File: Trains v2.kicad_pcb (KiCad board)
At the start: 2 copper layers, 200 x 50 mm, 28 parts, among them SW1 SW_SPST4, SW2 SW_SPST4

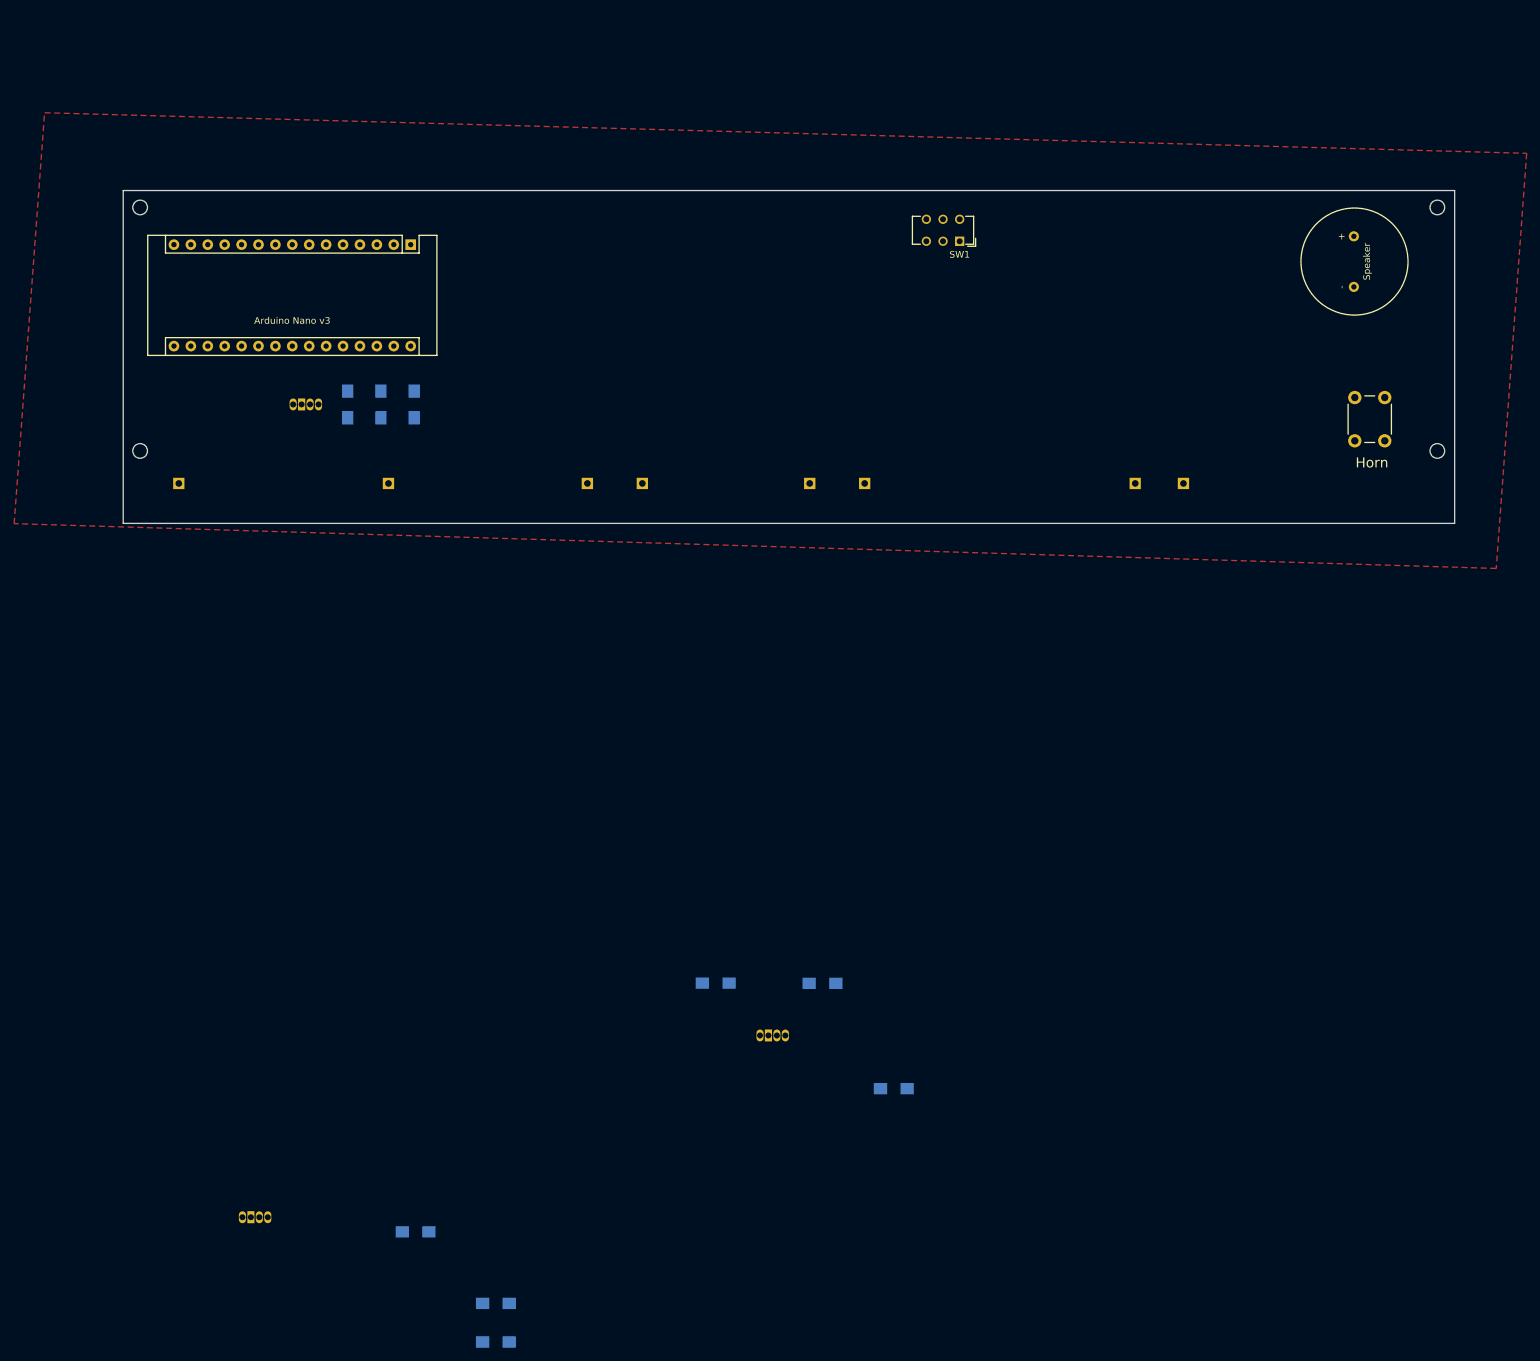
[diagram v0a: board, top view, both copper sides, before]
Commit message: Add & Align Pins
Add pins to all trains and set proper locations
Move RGB LEDs and resistors
Connect RGB LEDs to resistors and speaker to Arduino
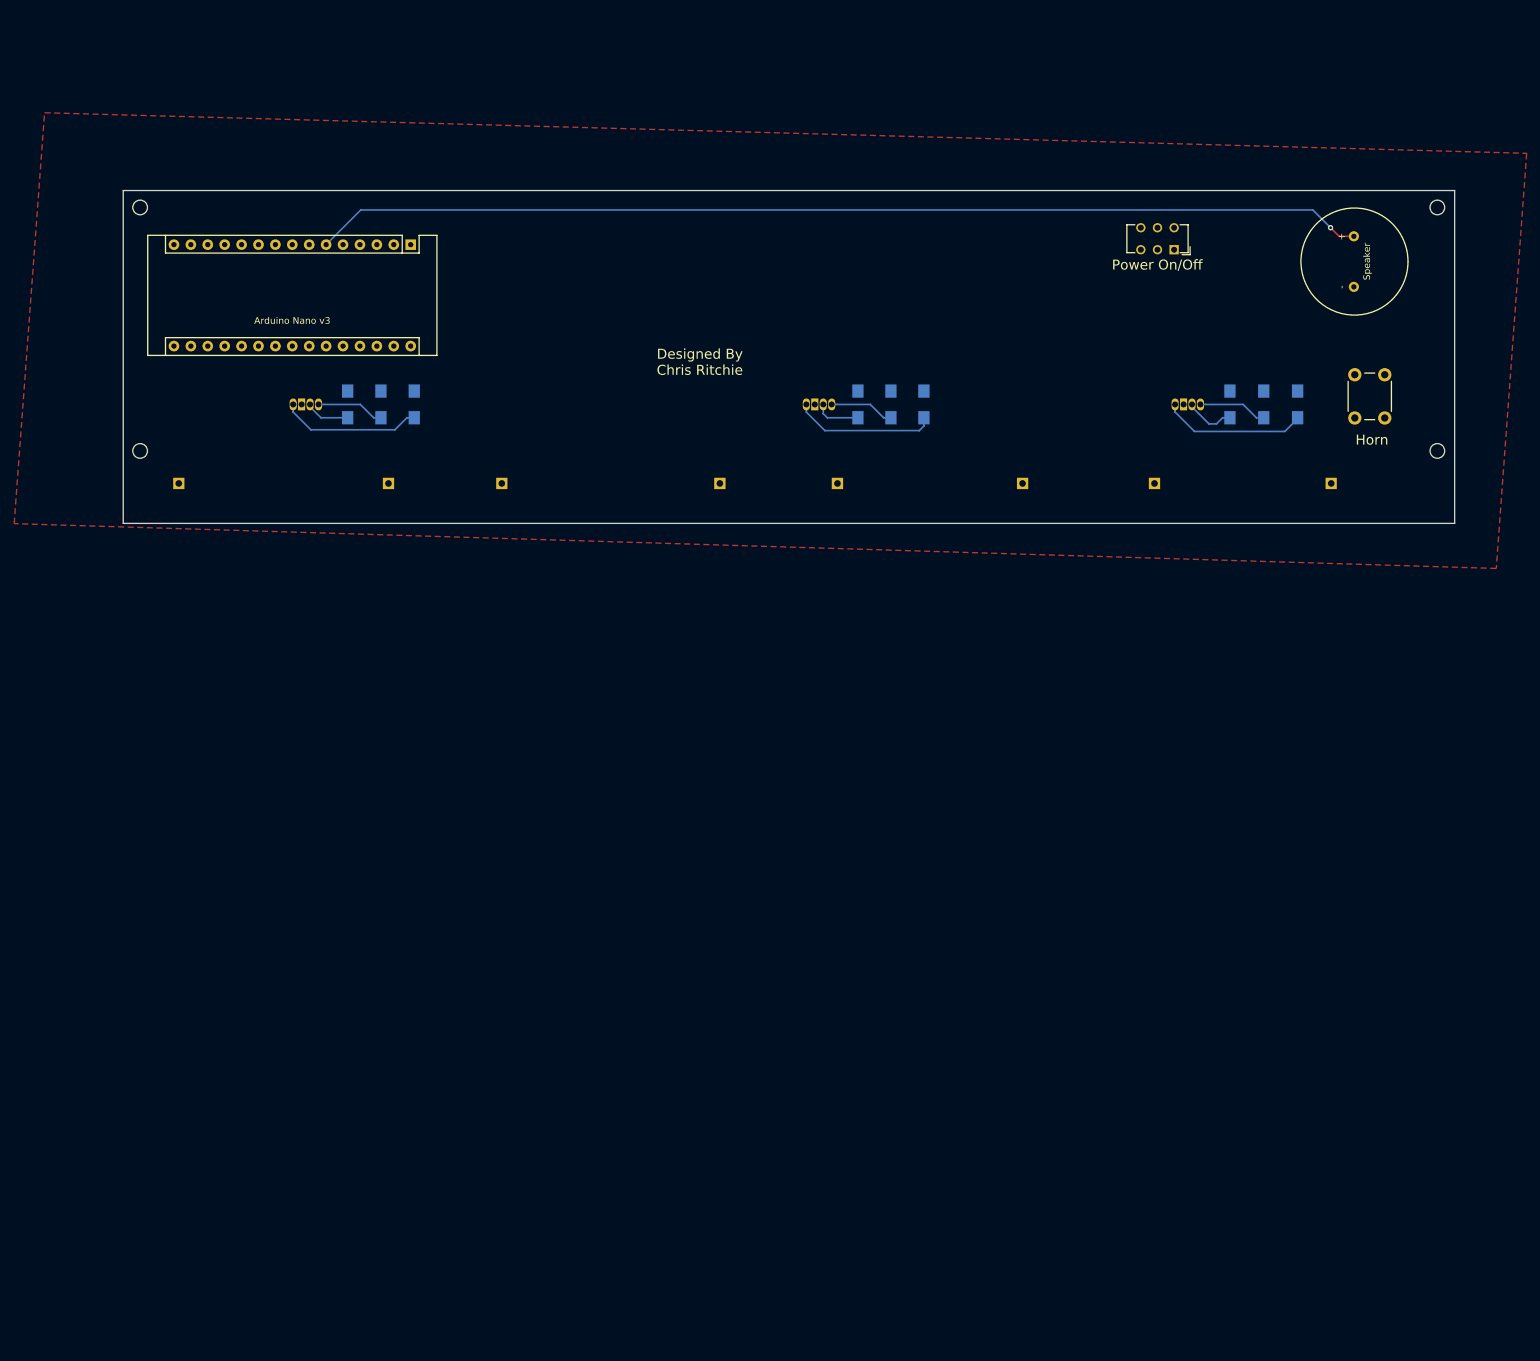
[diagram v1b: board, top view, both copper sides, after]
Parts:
- added G***: LOGO, logo:logoSolder, F.Cu at (80.0, 22.2)
- SW1: footprint Buttons_Switches_THT:SW_CuK_JS202011AQN_DPDT_Angled -> Buttons_Switches_THT:SW_CuK_JS202011CQN_DPDT_Straight
- moved R4 151.0 mm to (110.4, 32.1), turned to 90 degrees
- moved R6 149.6 mm to (120.3, 32.1), turned to 90 degrees
- moved D2 148.6 mm to (102.6, 32.1)
- moved R5 143.3 mm to (115.3, 32.1), turned to 90 degrees
- moved R9 119.3 mm to (176.4, 32.1), turned to 90 degrees
- moved R7 116.3 mm to (166.2, 32.1), turned to 90 degrees
- moved D3 113.5 mm to (158.0, 32.1)
- moved R8 109.3 mm to (171.3, 32.1), turned to 90 degrees
- moved SW1 32.2 mm to (157.9, 8.89)
- moved MK6 32.0 mm to (135.1, 44.0)
- moved MK8 29.4 mm to (181.5, 44.0)
- moved MK3 21.1 mm to (56.9, 44.0)
- moved MK4 19.9 mm to (89.6, 44.0)
- moved R1 5.00 mm to (33.7, 32.1)
- moved R2 5.00 mm to (38.7, 32.1)
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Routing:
- net /Speaker_Pin: track 0.00 -> 158.2 mm, vias 0 -> 1
- net Net-(D3-Pad1): track 0.00 -> 21.7 mm
- net Net-(D2-Pad1): track 0.00 -> 21.5 mm
- net Net-(D1-Pad1): track 0.00 -> 21.2 mm
- net Net-(D3-Pad4): track 0.00 -> 10.3 mm
- net Net-(D1-Pad4): track 0.00 -> 10.2 mm
- net Net-(D2-Pad4): track 0.00 -> 9.72 mm
- net Net-(D3-Pad3): track 0.00 -> 7.50 mm
- net Net-(D2-Pad3): track 0.00 -> 6.85 mm
- net Net-(D1-Pad3): track 0.00 -> 6.69 mm
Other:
- board text added: "100Ω"
- board text added: "47Ω"
- board text added: "Designed By Chris Ritchie"
- board text added: "Power On/Off"

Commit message: Connect Trains
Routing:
- net /Speaker_Button: track 0.00 -> 166.6 mm, vias 0 -> 1
- net /Boxcar_LED: track 0.00 -> 163.0 mm, vias 0 -> 1
- net /Caboose_LED: track 0.00 -> 71.7 mm, vias 0 -> 1
- net /Engine_LED: track 0.00 -> 20.9 mm
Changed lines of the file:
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@@
-(kicad_pcb (version 20171130) (host pcbnew 5.0.0-rc2-dev-unknown-1ac905d~64~ubuntu16.04.1)
+(kicad_pcb (version 20171130) (host pcbnew 5.0.0-rc2-dev-unknown-1f5b575~64~ubuntu16.04.1)
   (general
     (thickness 1.6)
     (drawings 18)
-    (tracks 44)
+    (tracks 64)
     (zones 0)
     (modules 29)
@@
   (gr_line (start 0 0) (end 200 0) (layer Edge.Cuts) (width 0.15))
   (gr_line (start 0 0) (end 0 50) (layer Edge.Cuts) (width 0.15))
+  (segment (start 7.62 43.27) (end 8.35 44) (width 0.25) (layer B.Cu) (net 1))
+  (segment (start 7.62 23.368) (end 7.62 43.27) (width 0.25) (layer B.Cu) (net 1))
+  (via (at 13.589 15.621) (size 0.8) (drill 0.4) (layers F.Cu B.Cu) (net 2))
+  (segment (start 125.435 15.621) (end 13.589 15.621) (width 0.25) (layer F.Cu) (net 2))
+  (segment (start 153.814 44) (end 125.435 15.621) (width 0.25) (layer F.Cu) (net 2))
+  (segment (start 154.914 44) (end 153.814 44) (width 0.25) (layer F.Cu) (net 2))
+  (segment (start 13.589 14.097) (end 7.62 8.128) (width 0.25) (layer B.Cu) (net 2))
+  (segment (start 13.589 15.621) (end 13.589 14.097) (width 0.25) (layer B.Cu) (net 2))
+  (segment (start 51.39 39.624) (end 18.923 39.624) (width 0.25) (layer F.Cu) (net 7))
+  (segment (start 55.766 44) (end 51.39 39.624) (width 0.25) (layer F.Cu) (net 7))
+  (via (at 18.923 39.624) (size 0.8) (drill 0.4) (layers F.Cu B.Cu) (net 7))
+  (segment (start 56.866 44) (end 55.766 44) (width 0.25) (layer F.Cu) (net 7))
+  (segment (start 18.923 9.271) (end 17.78 8.128) (width 0.25) (layer B.Cu) (net 7))
+  (segment (start 18.923 39.624) (end 18.923 9.271) (width 0.25) (layer B.Cu) (net 7))
   (segment (start 182.646 6.878) (end 181.356 5.588) (width 0.25) (layer F.Cu) (net 9))
   (via (at 181.356 5.588) (size 0.8) (drill 0.4) (layers F.Cu B.Cu) (net 9))
@@
   (segment (start 35.687 2.921) (end 30.48 8.128) (width 0.25) (layer B.Cu) (net 9))
   (segment (start 178.689 2.921) (end 35.687 2.921) (width 0.25) (layer B.Cu) (net 9))
+  (segment (start 172.628002 13.335) (end 34.798 13.335) (width 0.25) (layer F.Cu) (net 10))
+  (segment (start 175.167 13.335) (end 172.628002 13.335) (width 0.25) (layer F.Cu) (net 10))
+  (via (at 34.798 13.335) (size 0.8) (drill 0.4) (layers F.Cu B.Cu) (net 10))
+  (segment (start 189.5 27.668) (end 175.167 13.335) (width 0.25) (layer F.Cu) (net 10))
+  (segment (start 34.798 9.906) (end 33.02 8.128) (width 0.25) (layer B.Cu) (net 10))
+  (segment (start 34.798 13.335) (end 34.798 9.906) (width 0.25) (layer B.Cu) (net 10))
   (segment (start 30.122 32.131) (end 29.337 32.131) (width 0.25) (layer B.Cu) (net 11))
   (segment (start 35.616 32.131) (end 30.122 32.131) (width 0.25) (layer B.Cu) (net 11))

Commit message: Change Schematic For RGB LEDs
Add transistors to control 3 RGB LEDs
Add Silkscreen detail to caboose
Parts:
- removed R7, R8, R9: R, Resistors_SMD:R_1206_HandSoldering
- added Q1: 2N3906, TO_SOT_Packages_THT:TO-92_Molded_Narrow, F.Cu at (92.0, -22.0)
- added Q2: 2N3906, TO_SOT_Packages_THT:TO-92_Molded_Narrow, F.Cu at (98.3, -22.0)
- added Q3: 2N3906, TO_SOT_Packages_THT:TO-92_Molded_Narrow, F.Cu at (104.7, -22.0)
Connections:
- A1 pad 27: (no net) -> /5V
- D1 pad 1: Net-(D1-Pad1) -> /R_OUT
- D1 pad 3: Net-(D1-Pad3) -> /B_OUT
- D1 pad 4: Net-(D1-Pad4) -> /G_OUT
- D2 pad 1: Net-(D2-Pad1) -> /R_OUT
- D2 pad 3: Net-(D2-Pad3) -> /B_OUT
- D2 pad 4: Net-(D2-Pad4) -> /G_OUT
- D3 pad 1: Net-(D3-Pad1) -> /R_OUT
- D3 pad 3: Net-(D3-Pad3) -> /B_OUT
- D3 pad 4: Net-(D3-Pad4) -> /G_OUT
- R1 pad 1: Net-(D1-Pad3) -> Net-(Q1-Pad3)
- R1 pad 2: /LED_B -> /R_OUT
- R2 pad 1: Net-(D1-Pad4) -> Net-(Q2-Pad3)
- R2 pad 2: /LED_G -> /G_OUT
- R3 pad 1: Net-(D1-Pad1) -> Net-(Q3-Pad3)
- R3 pad 2: /LED_R -> /B_OUT
- R4 pad 1: Net-(D2-Pad3) -> /LED_R
- R4 pad 2: /LED_B -> Net-(Q1-Pad2)
- R5 pad 1: Net-(D2-Pad4) -> /LED_G
- R5 pad 2: /LED_G -> Net-(Q2-Pad2)
- R6 pad 1: Net-(D2-Pad1) -> /LED_B
- R6 pad 2: /LED_R -> Net-(Q3-Pad2)
- SW1 pad 2: (no net) -> /GND
- SW1 pad 4: /GND -> /Power_Button
- SW1 pad 5: (no net) -> /GND
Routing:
- net /Power_Button: track 0.00 -> 129.6 mm
- net Net-(D3-Pad1): track 21.7 -> 0.00 mm
- net Net-(D3-Pad4): track 10.3 -> 0.00 mm
- net Net-(D3-Pad3): track 7.50 -> 0.00 mm

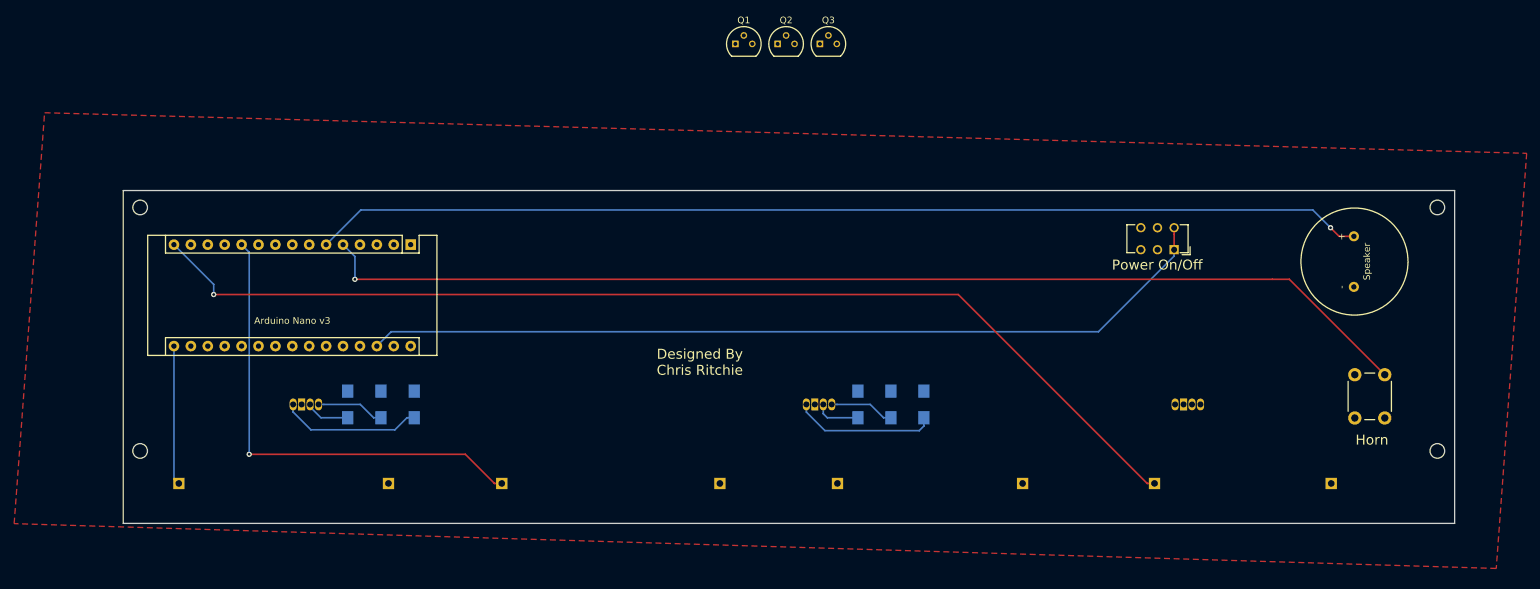
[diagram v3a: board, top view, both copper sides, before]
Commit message: Finalize Tracks
Finish tracks for 3 RGB LEDs
Move date to locomotive, remove from caboose
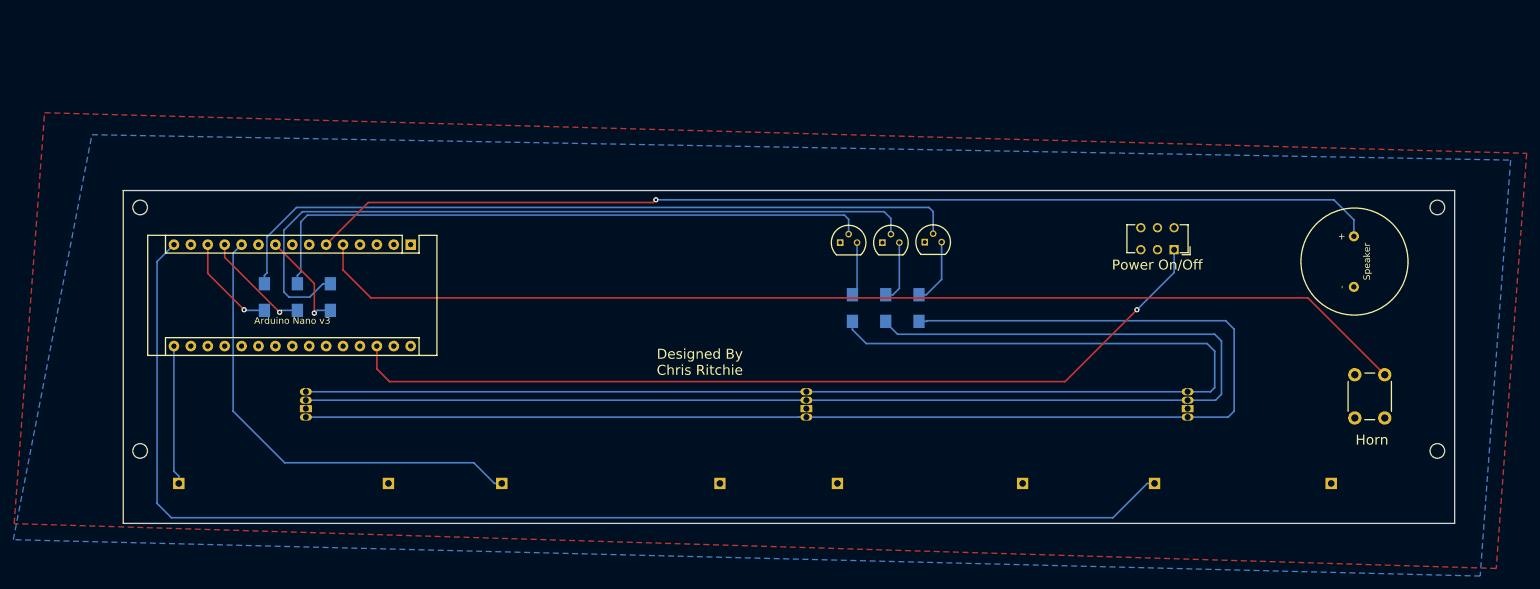
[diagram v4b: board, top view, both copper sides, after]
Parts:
- Q1, Q2, Q3: value 2N3906 -> 2N3904
- moved R6 90.6 mm to (31.1, 16.0)
- moved R4 90.6 mm to (21.2, 16.0)
- moved R5 90.6 mm to (26.2, 16.0)
- moved R1 87.0 mm to (119.5, 17.7), turned to 270 degrees
- moved R2 72.3 mm to (109.5, 17.7), turned to 270 degrees
- moved R3 72.3 mm to (114.5, 17.7), turned to 270 degrees
- moved Q1 41.2 mm to (120.4, 7.75)
- moved Q3 31.3 mm to (114.0, 7.82)
- moved Q2 31.3 mm to (107.7, 7.82)
- moved D1 2.69 mm to (27.4, 34.0), turned to 90 degrees
- moved D3 2.68 mm to (159.9, 34.0), turned to 90 degrees
- moved D2 1.91 mm to (102.6, 34.0), turned to 90 degrees
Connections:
- SW1 pad 2: /GND -> (no net)
- SW1 pad 4: /Power_Button -> /GND
- SW1 pad 5: /GND -> (no net)
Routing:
- net /R_OUT: track 0.00 -> 200.0 mm
- net /G_OUT: track 0.00 -> 199.3 mm
- net /B_OUT: track 0.00 -> 197.7 mm
- net Net-(Q1-Pad2): track 0.00 -> 112.7 mm
- net Net-(Q3-Pad2): track 0.00 -> 112.5 mm
- net Net-(Q2-Pad2): track 0.00 -> 94.7 mm
- net /Boxcar_LED: track 163.0 -> 192.8 mm, vias 1 -> 0
- net Net-(D2-Pad1): track 21.5 -> 0.00 mm
- net Net-(D1-Pad1): track 21.2 -> 0.00 mm
- net /LED_G: track 0.00 -> 16.4 mm, vias 0 -> 1
- net /LED_B: track 0.00 -> 15.3 mm, vias 0 -> 1
- net /LED_R: track 0.00 -> 15.1 mm, vias 0 -> 1
- net Net-(D1-Pad4): track 10.2 -> 0.00 mm
- net Net-(Q1-Pad3): track 0.00 -> 9.96 mm
- net Net-(D2-Pad4): track 9.72 -> 0.00 mm
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- added copper zone on B.Cu, net /5V
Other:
- board text added: "220Ω"
- board text added: "Add brd#"
- board text removed: "Add 2mm"
